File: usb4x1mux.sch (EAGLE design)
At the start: 44 parts, among them IC10 SN74LVC1G139DCTR, IC3 LDO5-3.3-SOT23, U1 LPC812M101JDH16

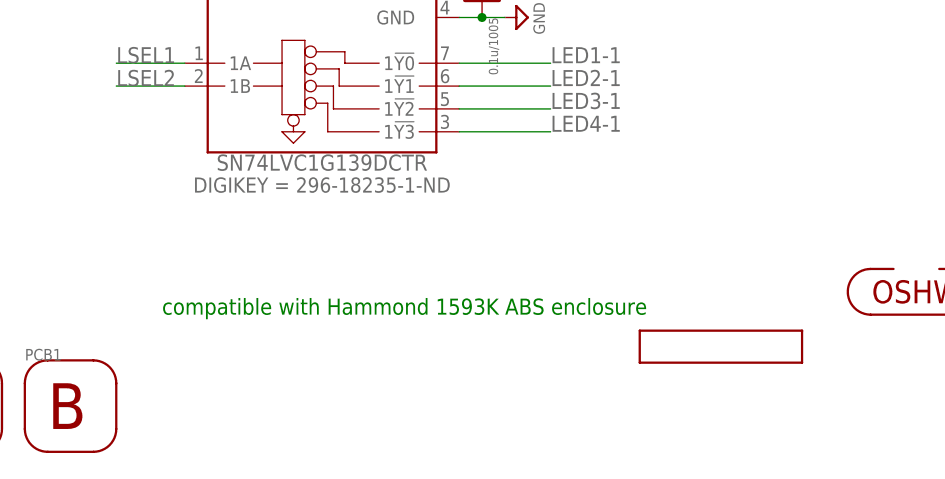
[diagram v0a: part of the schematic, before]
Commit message: update compatible enclosure list
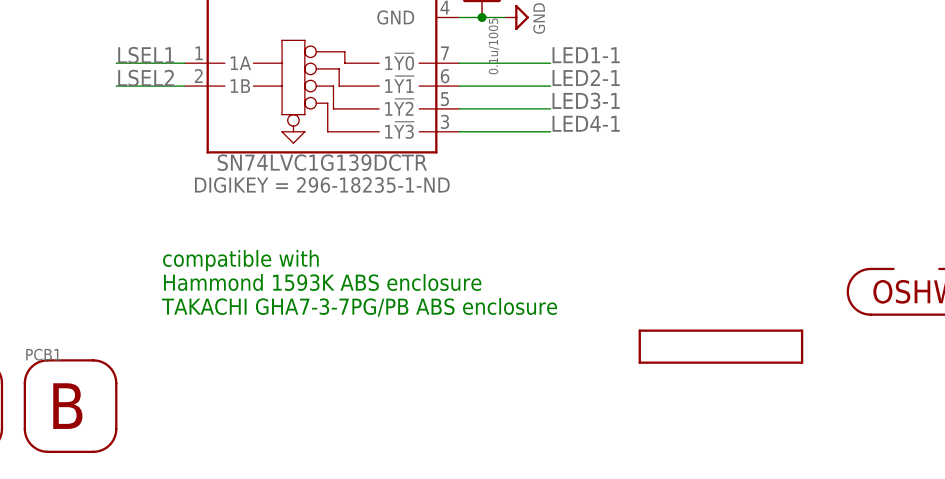
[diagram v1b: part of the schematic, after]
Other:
- note added: "compatible with Hammond 1593K ABS enclosure TAKACHI GHA7-3-7PG/PB ABS enclosure"
- note removed: "compatible with Hammond 1593K ABS enclosure"
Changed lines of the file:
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@@
 1B = P0_2
 </text>
-<text x="162.56" y="25.4" size="1.778" layer="91">compatible with Hammond 1593K ABS enclosure</text>
+<text x="162.56" y="25.4" size="1.778" layer="91">compatible with
+Hammond 1593K ABS enclosure
+TAKACHI GHA7-3-7PG/PB ABS enclosure</text>
 </plain>
 <instances>
